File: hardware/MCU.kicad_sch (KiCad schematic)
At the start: 71 parts, among them J1 Conn_ARM_JTAG_SWD_10, U1 ESP32-U4WDH, Y1 40MHz

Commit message: Updated schematic to add STM32
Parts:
- removed AE2: Antenna_Shield, symbol Device:Antenna_Shield
- removed C11: (no value), symbol Device:C
- removed C12: 3.3nF, symbol Device:C
- removed C13: 10nF, symbol Device:C
- removed C14, C15: 10pF, symbol Device:C
- removed C16, C17, C18, C3: 100nF, symbol Device:C
- removed L2, L3: 2nH, symbol Device:L
- removed R1: 20k, symbol Device:R_US
- removed R2: 0, symbol Device:R_US
- removed TP10, TP13, TP14, TP15, TP16, TP17, TP18, TP19, TP20, TP21, TP22, TP23, TP24, TP25, TP26, TP27, TP28, TP29, TP30, TP31, TP32, TP33, TP34, TP35, TP36, TP37, TP38, TP39, TP40, TP41, TP42, TP43, TP6, TP7, TP8, TP9: TestPoint, symbol Connector:TestPoint
- removed U1: ESP32-U4WDH, QFN48_5X5_EXP, symbol ESP32-U4WDH:ESP32-U4WDH
- removed Y1: 40MHz, symbol Device:Crystal
- added R4, R5: 1k, symbol Device:R_US
- added U1: STM32U595RJTxQ, Package_QFP:LQFP-64_10x10mm_P0.5mm, symbol MCU_ST_STM32U5:STM32U595RJTxQ
- C10, C9: value (none) -> 2.2uF
- C4: value 100nF -> 10uF
- C5: value 1uF -> 100nF
- C6: value 10uF -> 100nF
- C7: now fitted
- C8: value (none) -> 100nF
- L1: value 2nH -> L
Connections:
- net GND: now also C10.1, C9.1, R5.1, U1.12 (VSSA), U1.18 (VSS), U1.30 (VSSSMPS), U1.32 (VSS), U1.47 (VSS), U1.63 (VSS); no longer C10.2, C9.2
- net GPIO19 renamed eMMC/nRST
- net LNA_LN renamed +3V3
- net +3V3: now also C1.1, C2.1, C4.1, C5.1, C6.1, C7.1, J1.1 (VTref), R4.2, U1.1 (VBAT), U1.13 (VDDA), U1.19 (VDD), U1.29 (VDDSMPS), U1.33 (VDD), U1.48 (VDDUSB), U1.64 (VDD)
- net SD_CLK renamed eMMC/CLK
- net SD_CMD renamed eMMC/CMD
- removed net VDD: C1.1, C2.1, C4.1, C5.1, C6.1, J1.1 (VTref), L1.1
- net VDD3P3_FILT renamed VLXSMPS
- net VLXSMPS: now also U1.28 (VLXSMPS); no longer C7.1
- new net: R4.1, R5.2, U1.60 (PH3)
- new net VDD11: C10.2, C9.2, L1.1, U1.31 (VDD11), U1.62 (VDD11)
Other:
- note added: "Boot mode 1 - Bootloader 0x0BF9 0000 0 - Flash 0x0800 0000"
- note added: "PC14 OSC32_IN PC15 OSC32_OUT"
- note removed: "(Matching of antenna)"
- note removed: "(Matching of chip)"
- note removed: "DO NOT LEAVE FLOATING"
- note removed: "TEST POINTS"
- note removed: "XO"
- moved on the sheet: R3

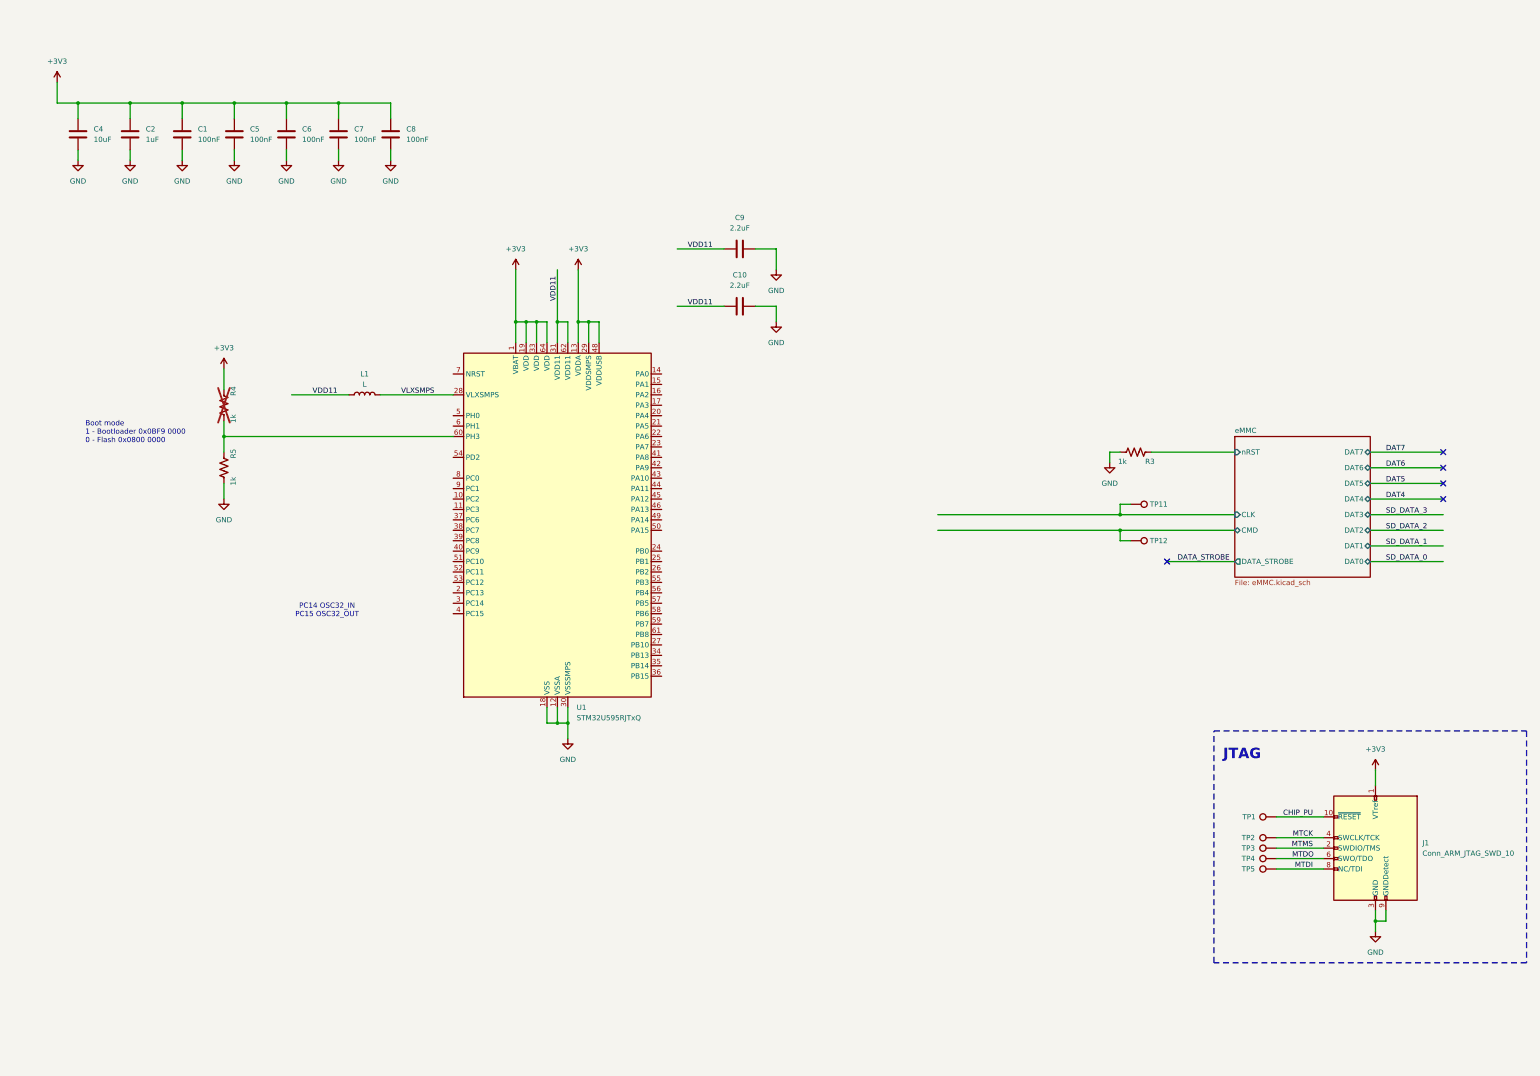
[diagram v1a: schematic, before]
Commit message: Abstracted STM32 into it's own schematic block and settled boot mode and reset scheme
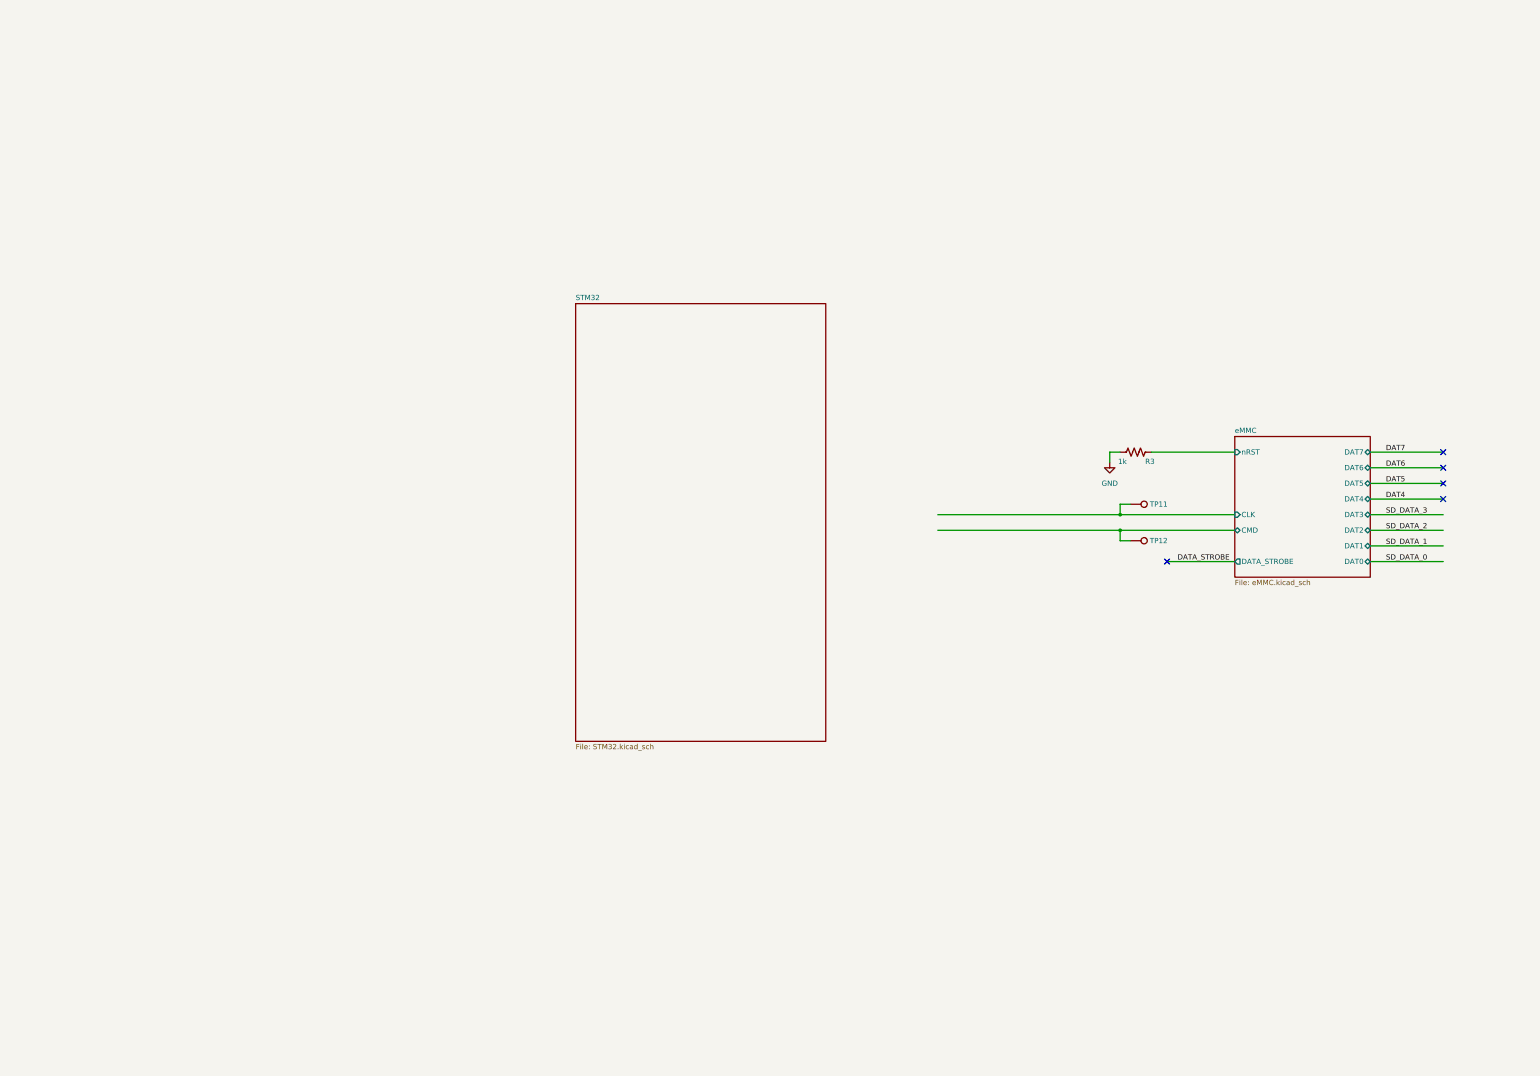
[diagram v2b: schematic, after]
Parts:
- removed C1, C5, C6, C7, C8: 100nF, symbol Device:C
- removed C10, C9: 2.2uF, symbol Device:C
- removed C2: 1uF, symbol Device:C
- removed C4: 10uF, symbol Device:C
- removed J1: Conn_ARM_JTAG_SWD_10, symbol Connector:Conn_ARM_JTAG_SWD_10
- removed L1: L, symbol Device:L
- removed R4, R5: 1k, symbol Device:R_US
- removed TP1, TP2, TP3, TP4, TP5: TestPoint, symbol Connector:TestPoint
- removed U1: STM32U595RJTxQ, Package_QFP:LQFP-64_10x10mm_P0.5mm, symbol MCU_ST_STM32U5:STM32U595RJTxQ
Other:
- added sheet STM32 (STM32.kicad_sch)
- note removed: "Boot mode 1 - Bootloader 0x0BF9 0000 0 - Flash 0x0800 0000"
- note removed: "JTAG"
- note removed: "PC14 OSC32_IN PC15 OSC32_OUT"

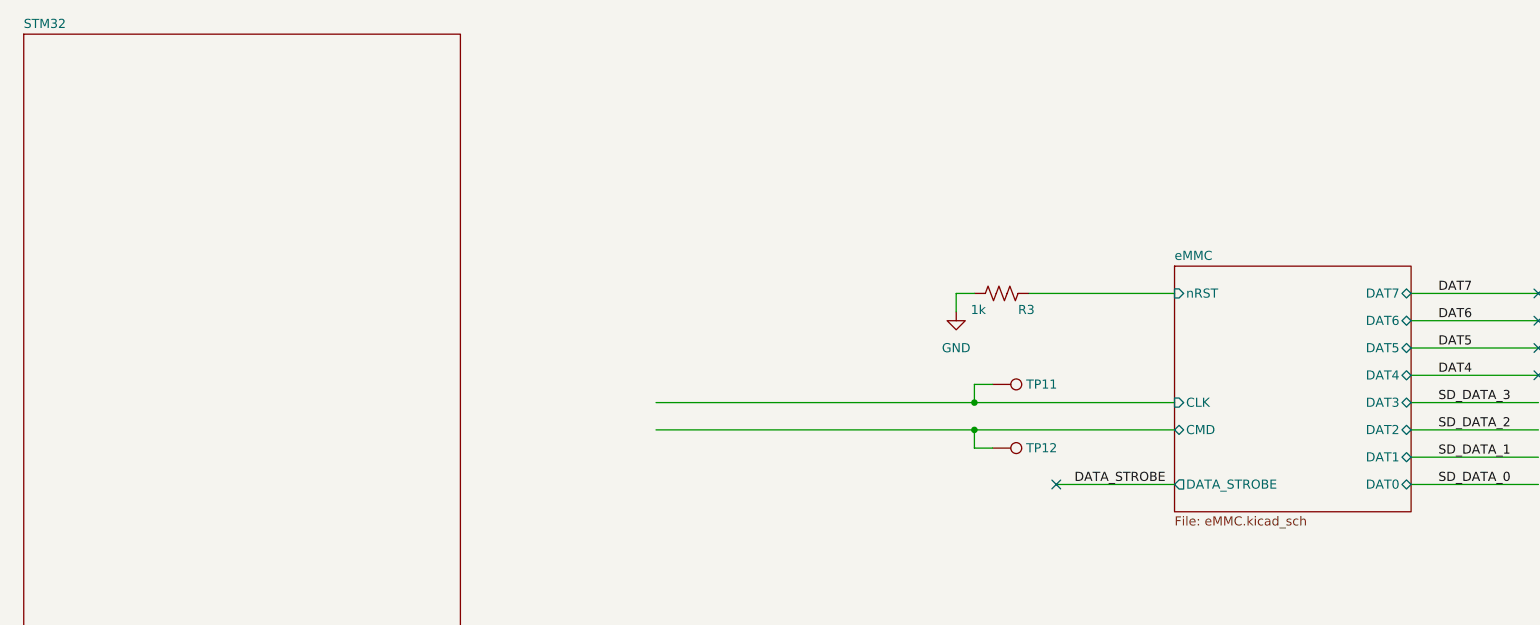
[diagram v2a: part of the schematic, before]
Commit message: Completed STM32 schematic
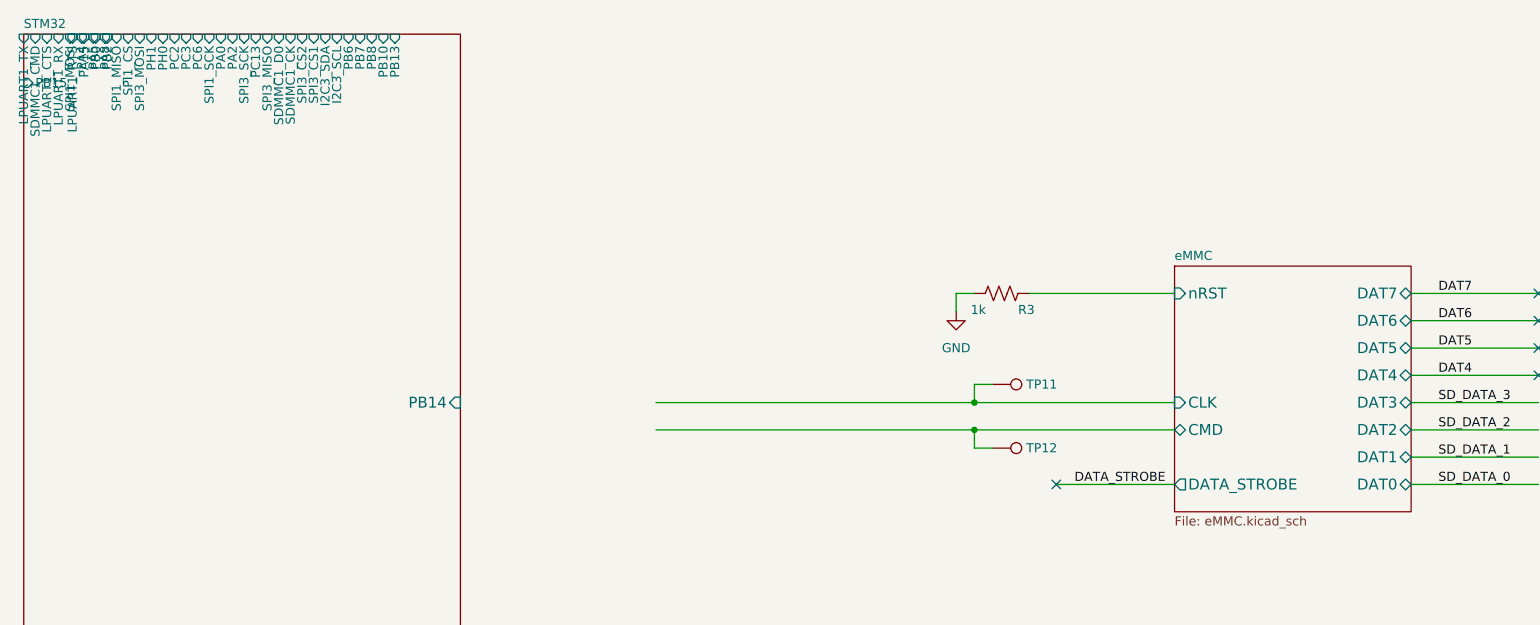
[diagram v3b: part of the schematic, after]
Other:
- sheet STM32 ports: added I2C3_SCL, I2C3_SDA, LPUART1_CTS, LPUART1_RTS, LPUART1_RX, LPUART1_TX, PA0, PA15, PA2, PA4, PA5, PA8, PB0, PB10, PB13, PB14, PB15, PB2, PB6, PB7, PB8, PC13, PC2, PC3, PC6, PH0, PH1, SDMMC1_CK, SDMMC1_CMD, SDMMC1_D0, SPI1_CS, SPI1_MISO, SPI1_MOSI, SPI1_SCK, SPI3_CS1, SPI3_CS2, SPI3_MISO, SPI3_MOSI, SPI3_SCK; removed none

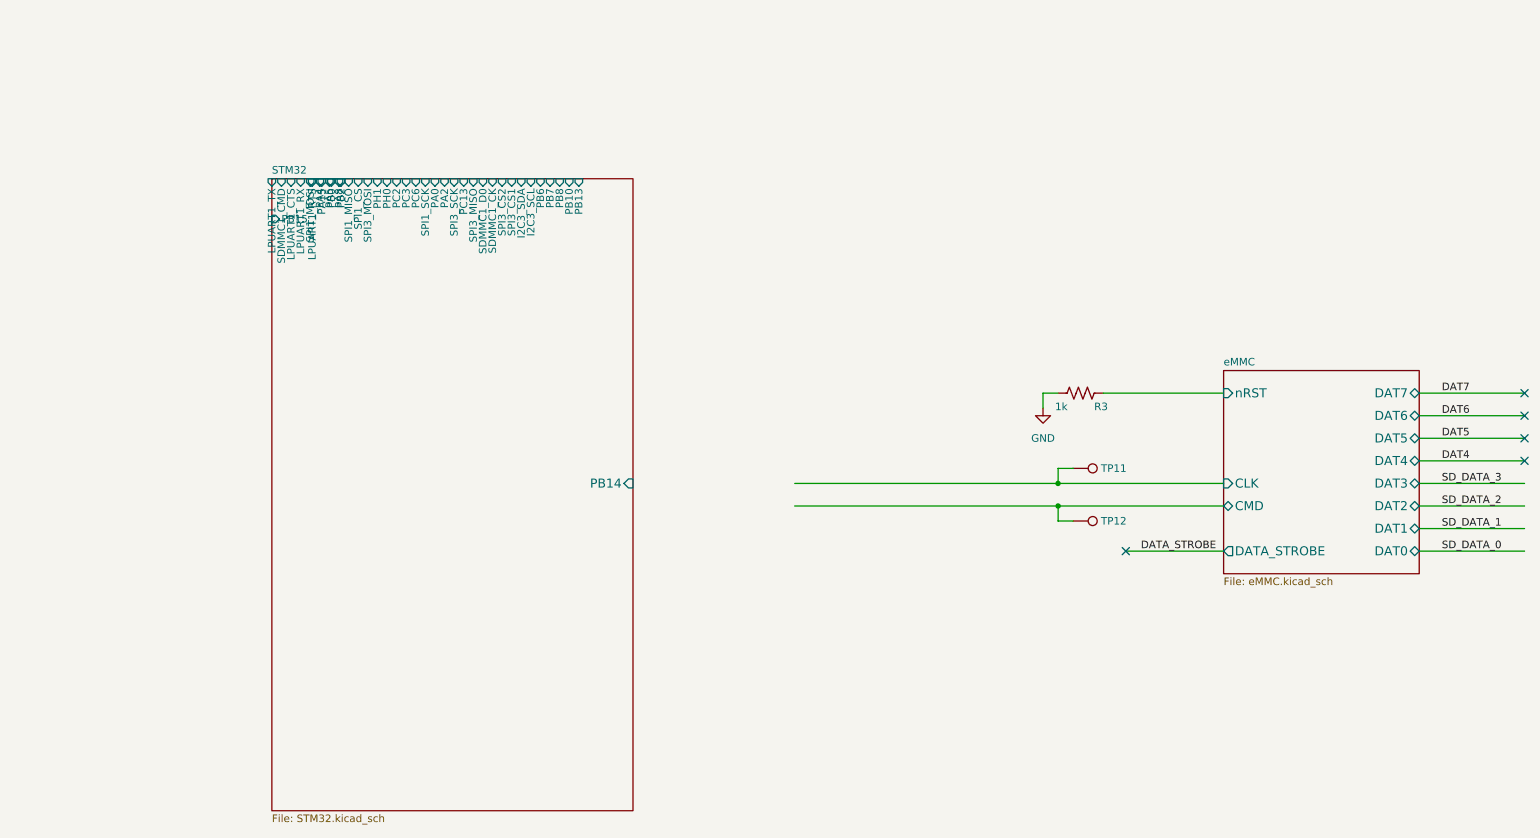
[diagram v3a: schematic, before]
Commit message: Completed STM32 high level block and connected eMMC
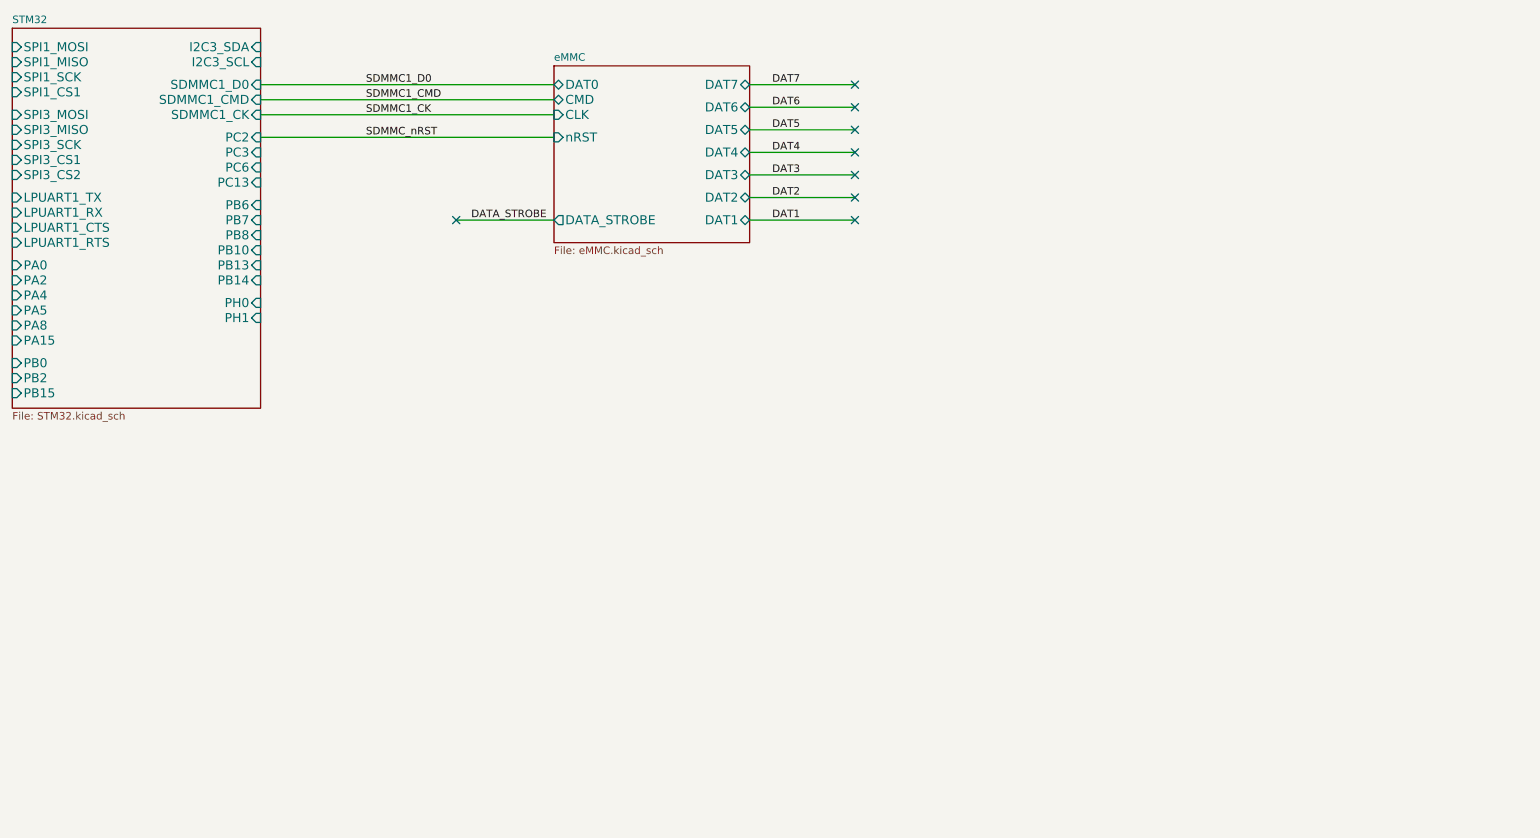
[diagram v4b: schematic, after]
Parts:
- removed R3: 1k, symbol Device:R_US
- removed TP11, TP12: TestPoint, symbol Connector:TestPoint
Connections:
- no-connect marks 5 -> 8
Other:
- sheet STM32 ports: added SPI1_CS1; removed SPI1_CS

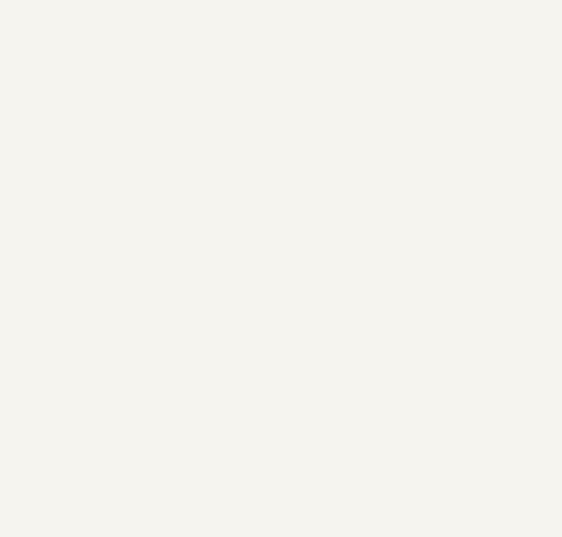
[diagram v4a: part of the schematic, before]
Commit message: Deleted GPS schematic to fit in compute sheet
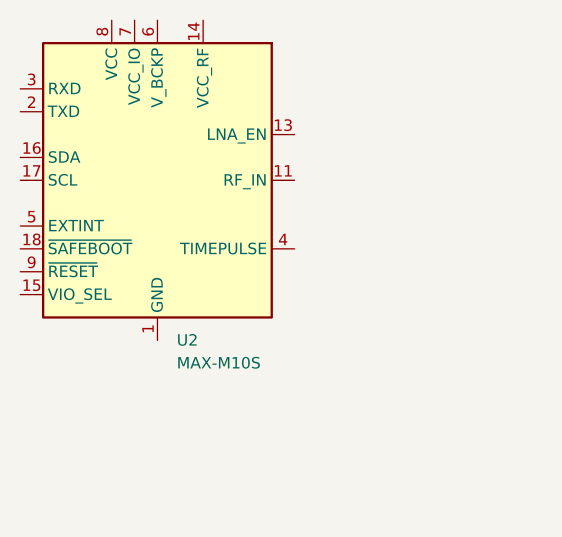
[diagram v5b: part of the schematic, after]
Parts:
- added U2: MAX-M10S, RF_GPS:ublox_MAX, symbol RF_GPS:MAX-M10S
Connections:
- new net: U2.1 (GND), U2.10 (GND), U2.12 (GND)
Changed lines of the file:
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@@
+		)
+	)
+	(symbol
+		(lib_id "RF_GPS:MAX-M10S")
+		(at 54.61 33.02 0)
+		(unit 1)
+		(body_style 1)
+		(exclude_from_sim no)
+		(in_bom yes)
+		(on_board yes)
+		(in_pos_files yes)
+		(dnp no)
+		(fields_autoplaced yes)
+		(property "Reference" "U2"
+			(at 56.7533 50.8 0)
+			(show_name no)
+			(do_not_autoplace no)
+			(effects
+				(font
+					(size 1.27 1.27)
+				)
+				(justify left)
+			)
+		)
+		(property "Value" "MAX-M10S"
+			(at 56.7533 53.34 0)
+			(show_name no)
+			(do_not_autoplace no)
+			(effects
+				(font
+					(size 1.27 1.27)
+				)
+				(justify left)
+			)
+		)
+		(property "Footprint" "RF_GPS:ublox_MAX"
+			(at 64.77 49.53 0)
+			(hide yes)
+			(show_name no)
+			(do_not_autoplace no)
+			(effects
+				(font
+					(size 1.27 1.27)
+				)
+			)
+		)
+		(property "Datasheet" "https://content.u-blox.com/sites/default/files/MAX-M10S_DataSheet_UBX-20035208.pdf"
+			(at 54.61 33.02 0)
+			(hide yes)
+			(show_name no)
+			(do_not_autoplace no)
+			(effects
+				(font
+					(size 1.27 1.27)
+				)
+			)
+		)
+		(property "Description" "GNSS Module MAX M10, VCC 1.65V to 3.6V"
+			(at 54.61 33.02 0)
+			(hide yes)
+			(show_name no)
+			(do_not_autoplace no)
+			(effects
+				(font
+					(size 1.27 1.27)
+				)
+			)
+		)
+		(pin "8"
+		)
+		(pin "7"
+		)
+		(pin "6"
+		)
+		(pin "5"
+		)
+		(pin "4"
+		)
+		(pin "11"
+		)
+		(pin "10"
+		)
+		(pin "9"
+		)
+		(pin "1"
+		)
+		(pin "2"
+		)
+		(pin "3"
+		)
+		(pin "12"
+		)
+		(pin "13"
+		)
+		(pin "14"
+		)
+		(pin "15"
+		)
+		(pin "16"
+		)
+		(pin "17"
+		)
+		(pin "18"
+		)
+		(instances
+			(project "hardware"
+				(path "/a19f636f-b28d-4c43-b96a-b02383edd3eb/66e2f96f-c2f9-49fe-949d-95863aff4e55"
+					(reference "U2")
+					(unit 1)
+				)
+			)
 		)
 	)
